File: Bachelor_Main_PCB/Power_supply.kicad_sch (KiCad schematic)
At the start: 18 parts, among them IC1 LD3985M18R, U10 LMR51450FNDRRR, U9 LM73100RPWR

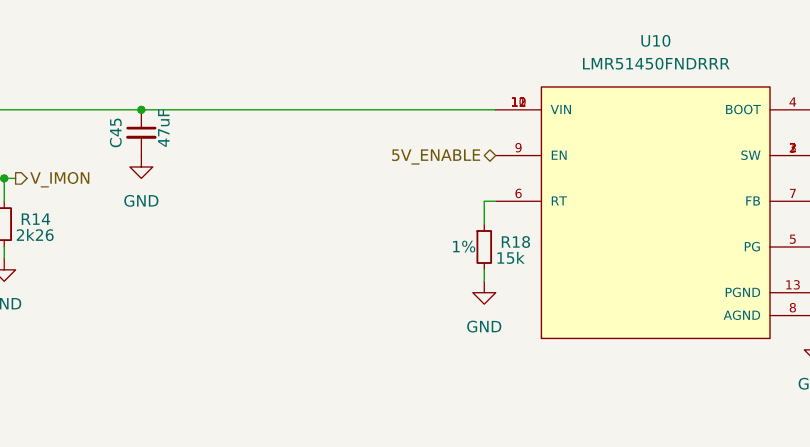
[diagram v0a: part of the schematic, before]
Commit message: Remove RPI CM power on mosfet. Replaced with EN pin to PSU
the pin is now routed instead to the LMR51450 converter ENABLE pin.
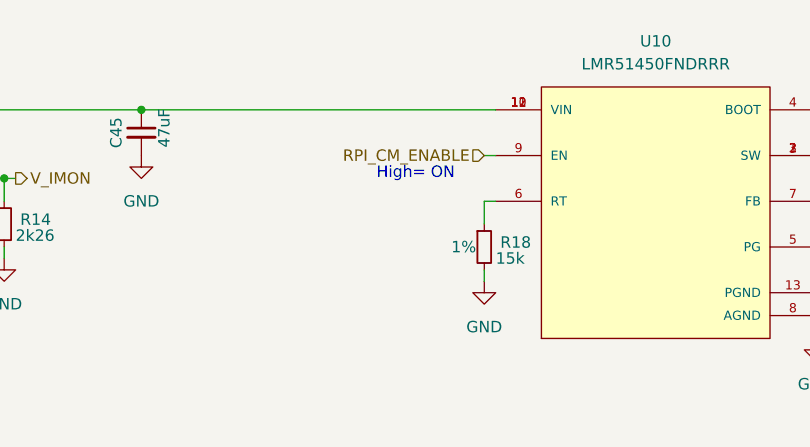
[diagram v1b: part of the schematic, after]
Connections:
- net 5V_ENABLE renamed RPI_CM_ENABLE
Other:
- note added: "High= ON"
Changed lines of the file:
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@@
+		)
+	)
+	(text "High= ON"
+		(exclude_from_sim no)
+		(at 148.59 32.512 0)
+		(effects
+			(font
+				(size 1.27 1.27)
+			)
 		)
 	)
@@
 		(pts
 			(xy 102.87 33.02) (xy 102.87 35.56)
+		)
+		(stroke
+			(width 0)
+			(type default)
+		)
+	)
+	(wire
+		(pts
+			(xy 156.21 30.48) (xy 157.48 30.48)
 		)
 		(stroke
@@
 		)
 	)
-	(hierarchical_label "5V_ENABLE"
-		(shape bidirectional)
-		(at 157.48 30.48 180)
+	(hierarchical_label "RPI_CM_ENABLE"
+		(shape input)
+		(at 156.21 30.48 180)
 		(effects
 			(font

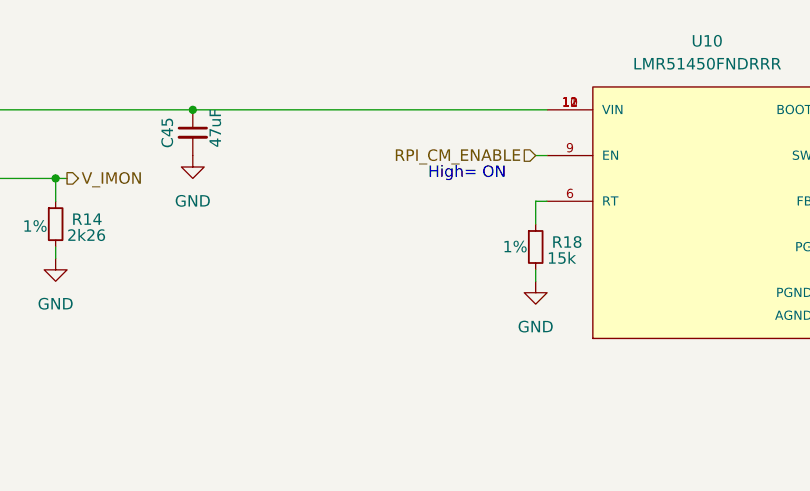
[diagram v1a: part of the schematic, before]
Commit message: add pulldown to PSU EN pin
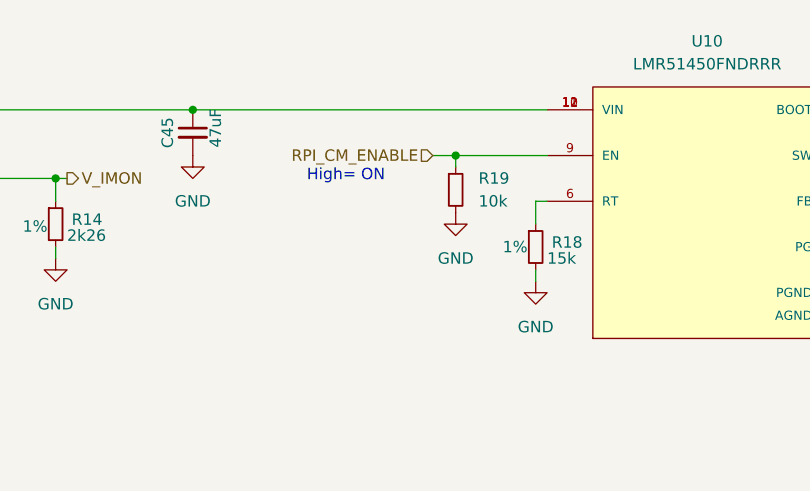
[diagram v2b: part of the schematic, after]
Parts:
- added R19: 10k, Resistor_SMD:R_0402_1005Metric, symbol Device:R_Small
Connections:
- net GND: now also R19.2
- net RPI_CM_ENABLE: now also R19.1
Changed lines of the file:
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@@
 	(text "High= ON"
 		(exclude_from_sim no)
-		(at 148.59 32.512 0)
+		(at 135.128 32.766 0)
 		(effects
 			(font
@@
 	)
 	(junction
+		(at 147.32 30.48)
+		(diameter 0)
+		(color 0 0 0 0)
+	)
+	(junction
 		(at 102.87 33.02)
 		(diameter 0)
@@
 	(wire
 		(pts
+			(xy 147.32 30.48) (xy 157.48 30.48)
+		)
+		(stroke
+			(width 0)
+			(type default)
+		)
+	)
+	(wire
+		(pts
 			(xy 251.46 29.21) (xy 251.46 24.13)
 		)
@@
 	(wire
 		(pts
+			(xy 147.32 31.75) (xy 147.32 30.48)
+		)
+		(stroke
+			(width 0)
+			(type default)
+		)
+	)
+	(wire
+		(pts
 			(xy 156.21 38.1) (xy 156.21 35.56)
 		)
@@
 	(wire
 		(pts
-			(xy 156.21 30.48) (xy 157.48 30.48)
+			(xy 144.78 30.48) (xy 147.32 30.48)
 		)
 		(stroke
@@
 	(hierarchical_label "RPI_CM_ENABLE"
 		(shape input)
-		(at 156.21 30.48 180)
+		(at 144.78 30.48 180)
 		(effects
 			(font
@@
 	(symbol
 		(lib_id "power:GND")
+		(at 147.32 36.83 0)
+		(unit 1)
+		(exclude_from_sim no)
+		(in_bom yes)
+		(on_board yes)
+		(dnp no)
+		(fields_autoplaced yes)
+		(property "Reference" "#PWR058"
+			(at 147.32 43.18 0)
+			(effects
+				(font
+					(size 1.27 1.27)
+				)
+				(hide yes)
+			)
+		)
+		(property "Value" "GND"
+			(at 147.32 41.91 0)
+			(effects
+				(font
+					(size 1.27 1.27)
+				)
+			)
+		)
+		(property "Footprint" ""
+			(at 147.32 36.83 0)
+			(effects
+				(font
+					(size 1.27 1.27)
+				)
+				(hide yes)
+			)
+		)
+		(property "Datasheet" ""
+			(at 147.32 36.83 0)
+			(effects
+				(font
+					(size 1.27 1.27)
+				)
+				(hide yes)
+			)
+		)
+		(property "Description" "Power symbol creates a global label with name \"GND\" , ground"
+			(at 147.32 36.83 0)
+			(effects
+				(font
+					(size 1.27 1.27)
+				)
+				(hide yes)
+			)
+		)
+		(pin "1"
+		)
+		(instances
+			(project "Bachelor_Main_PCB"
+				(path "/3544d663-329e-4884-b753-28436ca187e8/4408de3e-a395-4433-a2e1-ccefac59f96e"
+					(reference "#PWR058")
+					(unit 1)
+				)
+			)
+		)
+	)
+	(symbol
+		(lib_id "power:GND")
 		(at 294.64 33.02 0)
 		(unit 1)
@@
 					(unit 1)
 				)
+			)
+		)
+	)
+	(symbol
+		(lib_id "Device:R_Small")
+		(at 147.32 34.29 0)
+		(unit 1)
+		(exclude_from_sim no)
+		(in_bom yes)
+		(on_board yes)
+		(dnp no)
+		(fields_autoplaced yes)
+		(property "Reference" "R19"
+			(at 149.86 33.0199 0)
+			(effects
+				(font
+					(size 1.27 1.27)
+				)
+				(justify left)
+			)
+		)
+		(property "Value" "10k"
+			(at 149.86 35.5599 0)
+			(effects
+				(font
+					(size 1.27 1.27)
+				)
+				(justify left)
+			)
+		)
+		(property "Footprint" "Resistor_SMD:R_0402_1005Metric"
+			(at 147.32 34.29 0)
+			(effects
+				(font
+					(size 1.27 1.27)
+				)
+				(hide yes)
+			)
+		)
+		(property "Datasheet" "~"
+			(at 147.32 34.29 0)
+			(effects
+				(font
+					(size 1.27 1.27)
+				)
+				(hide yes)
+			)
+		)
+		(property "Description" "Resistor, small symbol"
+			(at 147.32 34.29 0)
+			(effects
+				(font
+					(size 1.27 1.27)
+				)
+				(hide yes)
+			)
+		)
+		(pin "1"
+		)
+		(pin "2"
+		)
+		(instances
+			(project "Bachelor_Main_PCB"
+				(path "/3544d663-329e-4884-b753-28436ca187e8/4408de3e-a395-4433-a2e1-ccefac59f96e"
+					(reference "R19")
+					(unit 1)
+				)

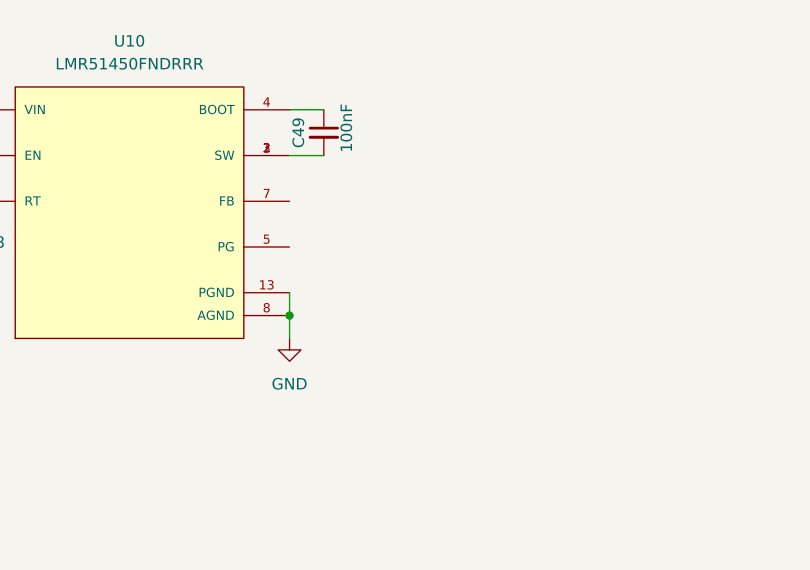
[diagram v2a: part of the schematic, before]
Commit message: Add voltage select divider
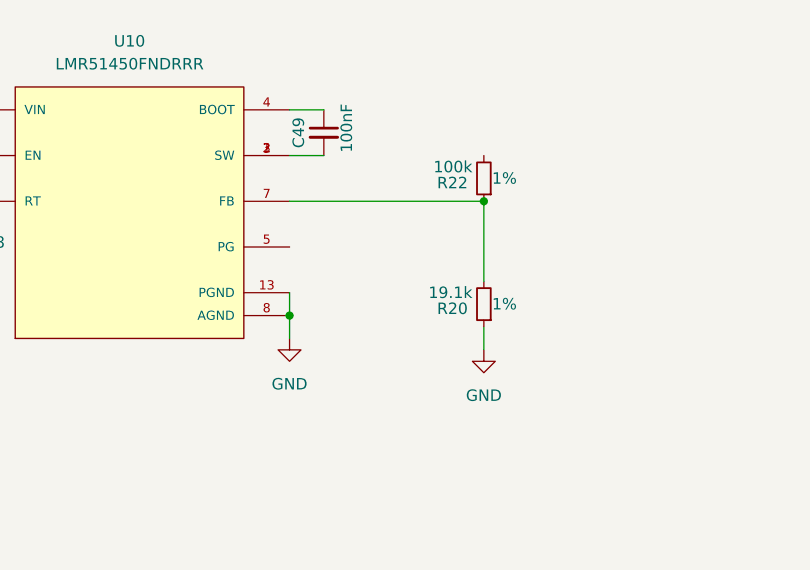
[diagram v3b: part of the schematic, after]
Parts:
- added R20: 19.1k, Resistor_SMD:R_0402_1005Metric, symbol Device:R_Small
- added R22: 100k, Resistor_SMD:R_0402_1005Metric, symbol Device:R_Small
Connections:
- net GND: now also R20.1
- net at U10.7 (FB): now also R20.2, R22.1

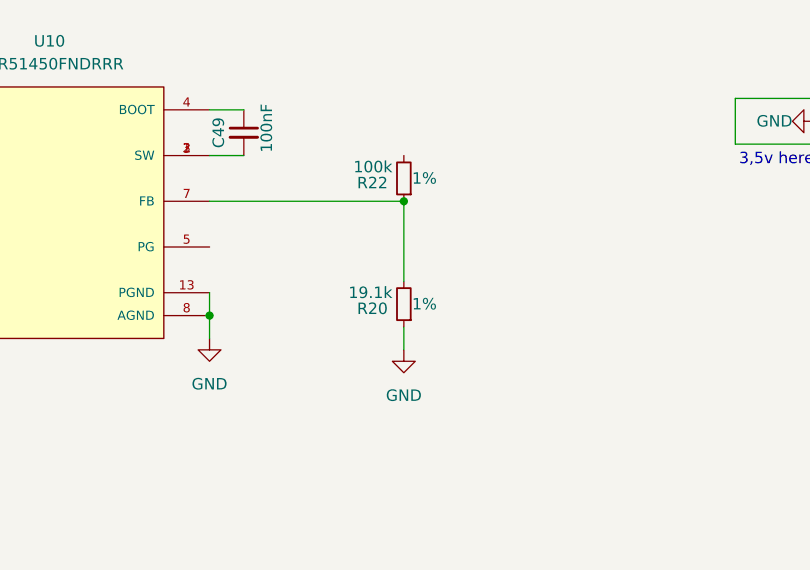
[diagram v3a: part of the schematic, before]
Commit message: add 4,7uH switchmode inductor
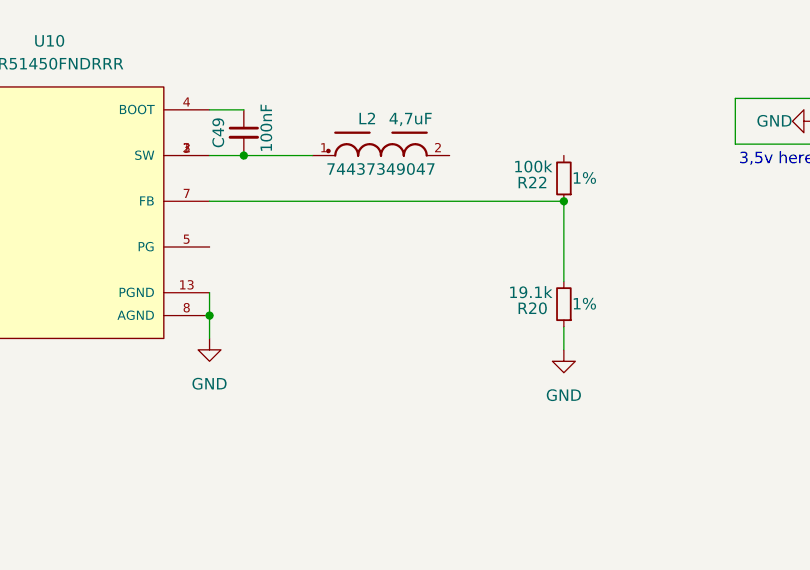
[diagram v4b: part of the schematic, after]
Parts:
- added L2: 4,7uF, WE-LHMI_7050:WE-LHMI_7050, symbol WE-LHMI_7050:WE-LHMI_7050
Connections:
- net at C49.2, U10.1 (SW), U10.2 (SW)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: now also L2.1
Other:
- moved on the sheet: R20, R22
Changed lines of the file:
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@@
 	)
 	(junction
-		(at 214.63 35.56)
+		(at 232.41 35.56)
 		(diameter 0)
 		(color 0 0 0 0)
@@
 		(color 0 0 0 0)
 	)
+	(junction
+		(at 196.85 30.48)
+		(diameter 0)
+		(color 0 0 0 0)
+	)
 	(no_connect
 		(at 58.42 35.56)
@@
 	(wire
 		(pts
-			(xy 214.63 44.45) (xy 214.63 35.56)
+			(xy 232.41 44.45) (xy 232.41 35.56)
 		)
 		(stroke
@@
 	(wire
 		(pts
-			(xy 214.63 52.07) (xy 214.63 49.53)
+			(xy 232.41 52.07) (xy 232.41 49.53)
 		)
 		(stroke
@@
 	(wire
 		(pts
+			(xy 196.85 30.48) (xy 204.47 30.48)
+		)
+		(stroke
+			(width 0)
+			(type default)
+		)
+	)
+	(wire
+		(pts
 			(xy 45.72 40.64) (xy 45.72 41.91)
 		)
@@
 	(wire
 		(pts
-			(xy 193.04 35.56) (xy 214.63 35.56)
+			(xy 193.04 35.56) (xy 232.41 35.56)
 		)
 		(stroke
@@
 	)
 	(symbol
+		(lib_id "WE-LHMI_7050:WE-LHMI_7050")
+		(at 212.09 30.48 0)
+		(unit 1)
+		(exclude_from_sim no)
+		(in_bom yes)
+		(on_board yes)
+		(dnp no)
+		(property "Reference" "L2"
+			(at 210.566 26.416 0)
+			(effects
+				(font
+					(size 1.27 1.27)
+				)
+			)
+		)
+		(property "Value" "4,7uF"
+			(at 215.392 26.416 0)
+			(effects
+				(font
+					(size 1.27 1.27)
+				)
+			)
+		)
+		(property "Footprint" "WE-LHMI_7050:WE-LHMI_7050"
+			(at 212.09 30.48 0)
+			(effects
+				(font
+					(size 1.27 1.27)
+				)
+				(justify bottom)
+				(hide yes)
+			)
+		)
+		(property "Datasheet" ""
+			(at 212.09 30.48 0)
+			(effects
+				(font
+					(size 1.27 1.27)
+				)
+				(hide yes)
+			)
+		)
+		(property "Description" ""
+			(at 212.09 30.48 0)
+			(effects
+				(font
+					(size 1.27 1.27)
+				)
+				(hide yes)
+			)
+		)
+		(property "MF" "Würth Elektronik"
+			(at 212.09 30.48 0)
+			(effects
+				(font
+					(size 1.27 1.27)
+				)
+				(justify bottom)
+				(hide yes)
+			)
+		)
+		(property "Description_1" "4.7µH Shielded Molded Inductor 5A 30.8mOhm Max Nonstandard"
+			(at 212.09 30.48 0)
+			(effects
+				(font
+					(size 1.27 1.27)
+				)
+				(justify bottom)
+				(hide yes)
+			)
+		)
+		(property "Package" "Nonstandard Würth Elektronik"
+			(at 212.09 30.48 0)
+			(effects
+				(font
+					(size 1.27 1.27)
+				)
+				(justify bottom)
+				(hide yes)
+			)
+		)
+		(property "Price" "None"
+			(at 212.09 30.48 0)
+			(effects
+				(font
+					(size 1.27 1.27)
+				)
+				(justify bottom)
+				(hide yes)
+			)
+		)
+		(property "SnapEDA_Link" "https://www.snapeda.com/parts/74437349047/W%25C3%25BCrth+Elektronik+Midcom/view-part/?ref=snap"
+			(at 212.09 30.48 0)
+			(effects
+				(font
+					(size 1.27 1.27)
+				)
+				(justify bottom)
+				(hide yes)
+			)
+		)
+		(property "MP" "74437349047"
+			(at 212.09 32.766 0)
+			(effects
+				(font
+					(size 1.27 1.27)
+				)
+				(justify bottom)
+			)
+		)
+		(property "Availability" "In Stock"
+			(at 212.09 30.48 0)
+			(effects
+				(font
+					(size 1.27 1.27)
+				)
+				(justify bottom)
+				(hide yes)
+			)
+		)
+		(property "Check_prices" "https://www.snapeda.com/parts/74437349047/W%25C3%25BCrth+Elektronik+Midcom/view-part/?ref=eda"
+			(at 212.09 30.48 0)
+			(effects
+				(font
+					(size 1.27 1.27)
+				)
+				(justify bottom)
+				(hide yes)
+			)
+		)
+		(pin "1"
+		)
+		(pin "2"
+		)
+		(instances
+			(project ""
+				(path "/3544d663-329e-4884-b753-28436ca187e8/4408de3e-a395-4433-a2e1-ccefac59f96e"
+					(reference "L2")
+					(unit 1)
+				)
+			)
+		)
+	)
+	(symbol
 		(lib_id "power:GND")
 		(at 260.35 26.67 270)
@@
 	(symbol
 		(lib_id "power:GND")
-		(at 214.63 52.07 0)
+		(at 232.41 52.07 0)
 		(unit 1)
 		(exclude_from_sim no)
@@
 		(fields_autoplaced yes)
 		(property "Reference" "#PWR059"
-			(at 214.63 58.42 0)
+			(at 232.41 58.42 0)
 			(effects
 				(font
@@
 		)
 		(property "Value" "GND"
-			(at 214.63 57.15 0)
+			(at 232.41 57.15 0)
 			(effects
 				(font
@@
 		)
 		(property "Footprint" ""
-			(at 214.63 52.07 0)
+			(at 232.41 52.07 0)
 			(effects
 				(font
@@
 		)
 		(property "Datasheet" ""
-			(at 214.63 52.07 0)
+			(at 232.41 52.07 0)
 			(effects
 				(font
@@
 		)
 		(property "Description" "Power symbol creates a global label with name \"GND\" , ground"
-			(at 214.63 52.07 0)
+			(at 232.41 52.07 0)
 			(effects
 				(font
@@
 	(symbol
 		(lib_id "Device:R_Small")
-		(at 214.63 33.02 180)
+		(at 232.41 33.02 180)
 		(unit 1)
 		(exclude_from_sim no)
@@
 		(dnp no)
 		(property "Reference" "R22"
-			(at 212.852 33.528 0)
+			(at 230.632 33.528 0)
 			(effects
 				(font
@@
 		)
 		(property "Value" "100k"
-			(at 213.36 31.75 0)
+			(at 231.14 31.75 0)
 			(effects
 				(font
@@
 		)
 		(property "Footprint" "Resistor_SMD:R_0402_1005Metric"
-			(at 214.63 33.02 0)
+			(at 232.41 33.02 0)
 			(effects
 				(font
@@
 		)
 		(property "Datasheet" "~"
-			(at 214.63 33.02 0)
+			(at 232.41 33.02 0)
 			(effects
 				(font
@@
 		)
 		(property "Description" "Resistor, small symbol"
-			(at 214.63 33.02 0)
+			(at 232.41 33.02 0)
 			(effects
 				(font
@@
 		)
 		(property "Tolerance" "1%"
-			(at 216.916 33.02 0)
+			(at 234.696 33.02 0)
 			(effects
 				(font
@@
 	(symbol
 		(lib_id "Device:R_Small")
-		(at 214.63 46.99 180)
+		(at 232.41 46.99 180)
 		(unit 1)
 		(exclude_from_sim no)
@@
 		(dnp no)
 		(property "Reference" "R20"
-			(at 212.852 47.498 0)
+			(at 230.632 47.498 0)
 			(effects
 				(font
@@
 		)
 		(property "Value" "19.1k"
-			(at 213.36 45.72 0)
+			(at 231.14 45.72 0)
 			(effects
 				(font
@@
 		)
 		(property "Footprint" "Resistor_SMD:R_0402_1005Metric"
-			(at 214.63 46.99 0)
+			(at 232.41 46.99 0)
 			(effects
 				(font
@@
 		)
 		(property "Datasheet" "~"
-			(at 214.63 46.99 0)
+			(at 232.41 46.99 0)
 			(effects
 				(font
@@
 		)
 		(property "Description" "Resistor, small symbol"
-			(at 214.63 46.99 0)
+			(at 232.41 46.99 0)
 			(effects
 				(font
@@
 		)
 		(property "Tolerance" "1%"
-			(at 216.916 46.99 0)
-			(effects
-				(font
+			(at 234.696 46.99 0)
+			(effects
+				(font
